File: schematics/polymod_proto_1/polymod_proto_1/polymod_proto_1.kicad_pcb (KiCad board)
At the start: 2 copper layers, 133 parts, among them J1 Conn_01x02_Male, J10 Conn_01x08_Male, J11 Conn_01x08_Male, J12 Conn_01x08_Male, J13 Conn_01x08_Male, J14 Conn_01x03_Male, J2 Conn_01x03_Male, J3 Conn_01x02_Male, J4 Barrel_Jack, J6 Conn_01x08_Male, J7 Conn_01x08_Male, J8 Conn_01x08_Male, J9 Conn_01x08_Male, SW1 SW_Push, SW2 SW_Push, SW3 SW_Push, SW4 SW_Push, U1 6N138, U10 74HC595, U11 74LS165, U12 74LS165, U13 74LS165, U2 74HC595, U3 74LS165, U4 4051, U5 74HC595, U6 74LS165, U7 4051, U8 74HC595, U9 74HC595

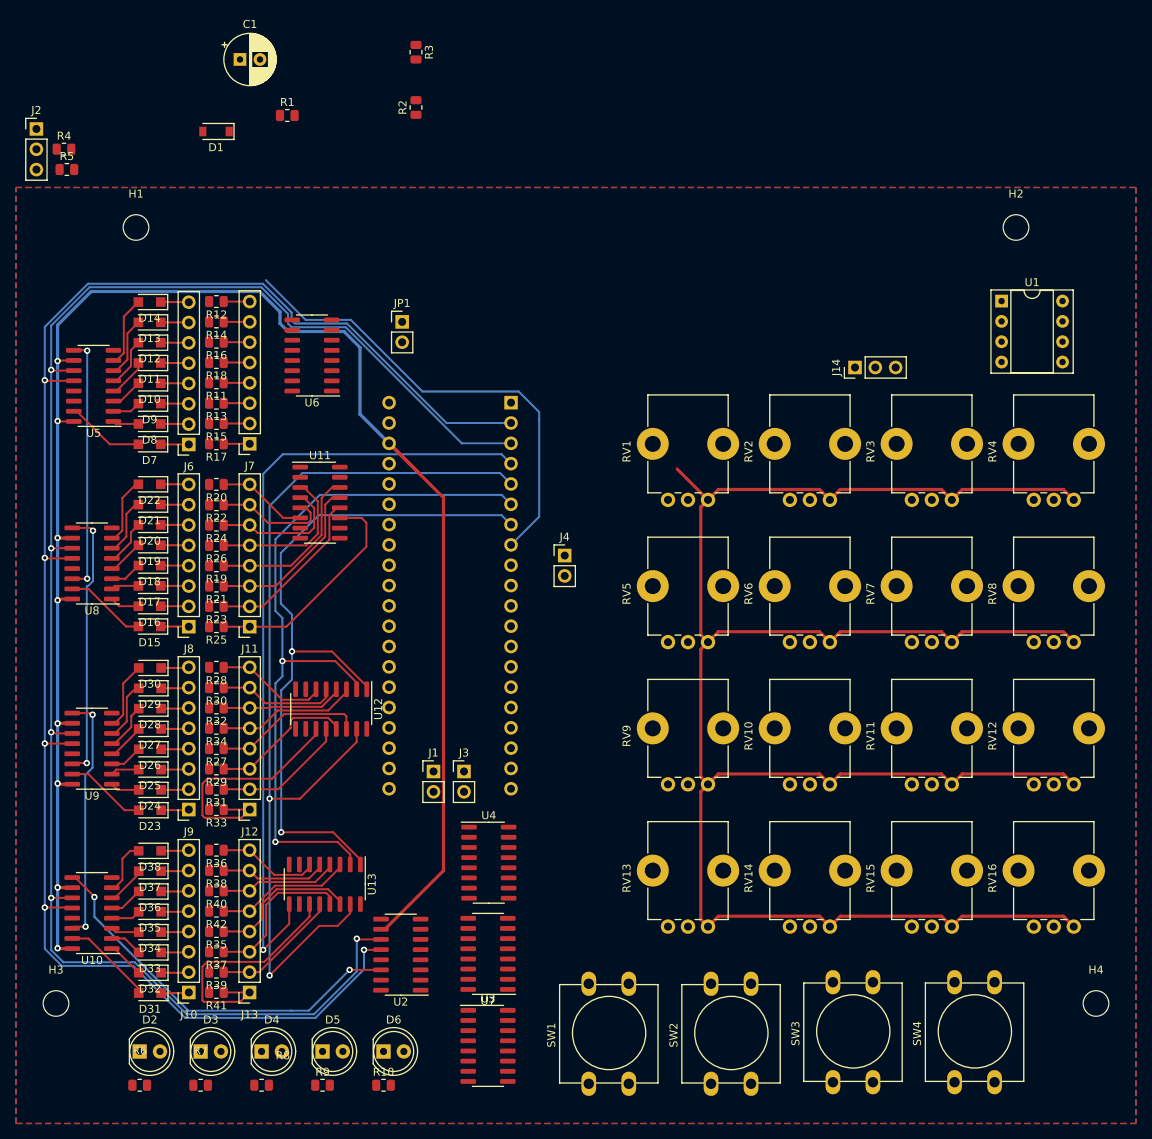
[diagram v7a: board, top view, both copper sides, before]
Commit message: reposition things for more efficient routing
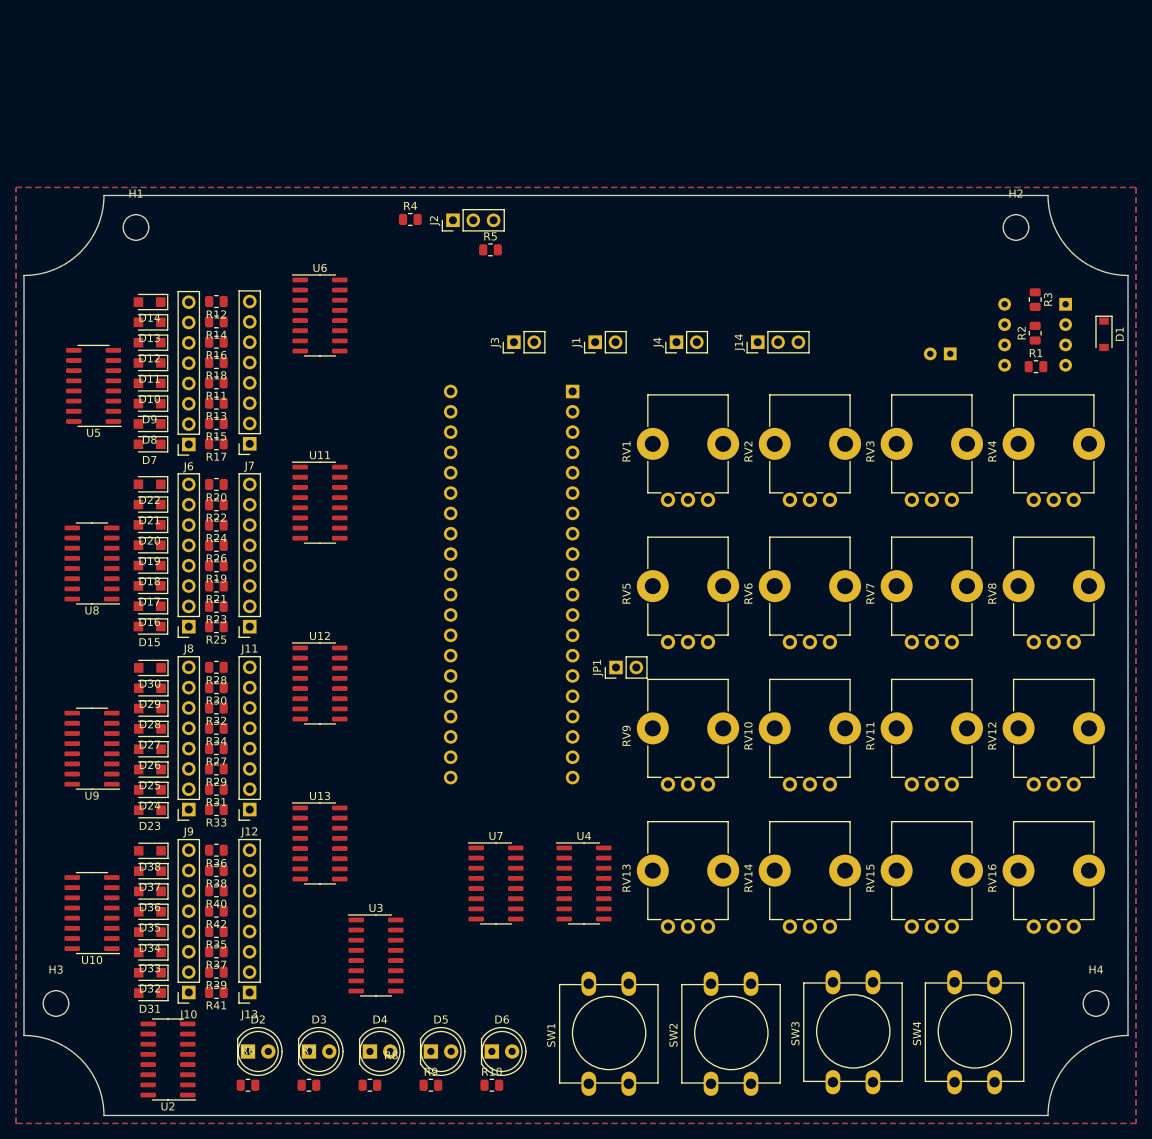
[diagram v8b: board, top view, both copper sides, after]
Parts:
- C1, U1: moved to B.Cu
- moved D1 113.9 mm to (216.0, 52.4), turned to -90 degrees
- moved R1 98.7 mm to (207.5, 56.4)
- moved C1 96.1 mm to (196.8, 54.8), turned to 180 degrees
- moved R3 83.3 mm to (207.4, 48.0)
- moved R2 82.4 mm to (207.4, 52.2)
- moved J1 57.3 mm to (152.4, 53.3), turned to 90 degrees
- moved J3 54.0 mm to (142.2, 53.3), turned to 90 degrees
- moved R5 53.9 mm to (139.3, 41.8)
- moved J2 53.3 mm to (134.6, 38.1), turned to 90 degrees
- moved JP1 50.8 mm to (155.0, 94.0), turned to 90 degrees
- moved R4 44.2 mm to (129.3, 38.0)
- moved U2 31.9 mm to (99.0, 143.0)
- moved J4 30.1 mm to (162.6, 53.3), turned to 90 degrees
- moved U3 18.0 mm to (125.0, 130.0)
- moved D5 13.5 mm to (131.9, 142.0)
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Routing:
- net VCC: track 479.3 -> 0.00 mm, vias 8 -> 0
- net PATCHING_OUT_LATCH: track 210.6 -> 0.00 mm, vias 5 -> 0
- net PATCHING_OUT_CLOCK: track 208.0 -> 0.00 mm, vias 5 -> 0
- net PATCHING_IN_CE: track 121.0 -> 0.00 mm, vias 2 -> 0
- net /PATCHING_IN_DATA: track 99.1 -> 0.00 mm, vias 1 -> 0
- net PATCHING_IN_CLOCK: track 93.3 -> 0.00 mm, vias 2 -> 0
- net PATCHING_IN_LOAD: track 90.8 -> 0.00 mm, vias 2 -> 0
- net /PATCHING_OUT_DATA: track 59.1 -> 0.00 mm
- net /UTIL_595: track 49.1 -> 0.00 mm, vias 2 -> 0
- net /Output group 2/OUTPUT: track 34.0 -> 0.00 mm, vias 2 -> 0
- net /Output group 1/OUTPUT: track 32.1 -> 0.00 mm, vias 2 -> 0
- net Net-(J13-Pad1): track 31.5 -> 0.00 mm
- net /Output group 3/OUTPUT: track 31.3 -> 0.00 mm, vias 2 -> 0
- net Net-(J12-Pad1): track 31.1 -> 0.00 mm
- net Net-(J11-Pad1): track 28.5 -> 0.00 mm
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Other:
- board outline added: 138 x 115 mm
